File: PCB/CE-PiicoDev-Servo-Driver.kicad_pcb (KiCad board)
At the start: 2 copper layers, 25.4 x 52 mm, 36 parts, among them J1 , J2 , J3 Conn_01x03_Male, J4 Conn_01x03_Male, J5 Conn_01x03_Male, J6 Conn_01x02_Male, J7 Conn_01x02_Male, J8 USB_C_Receptacle_USB2.0, J9 USB_C_Receptacle_USB2.0, U1 PCA9685PW

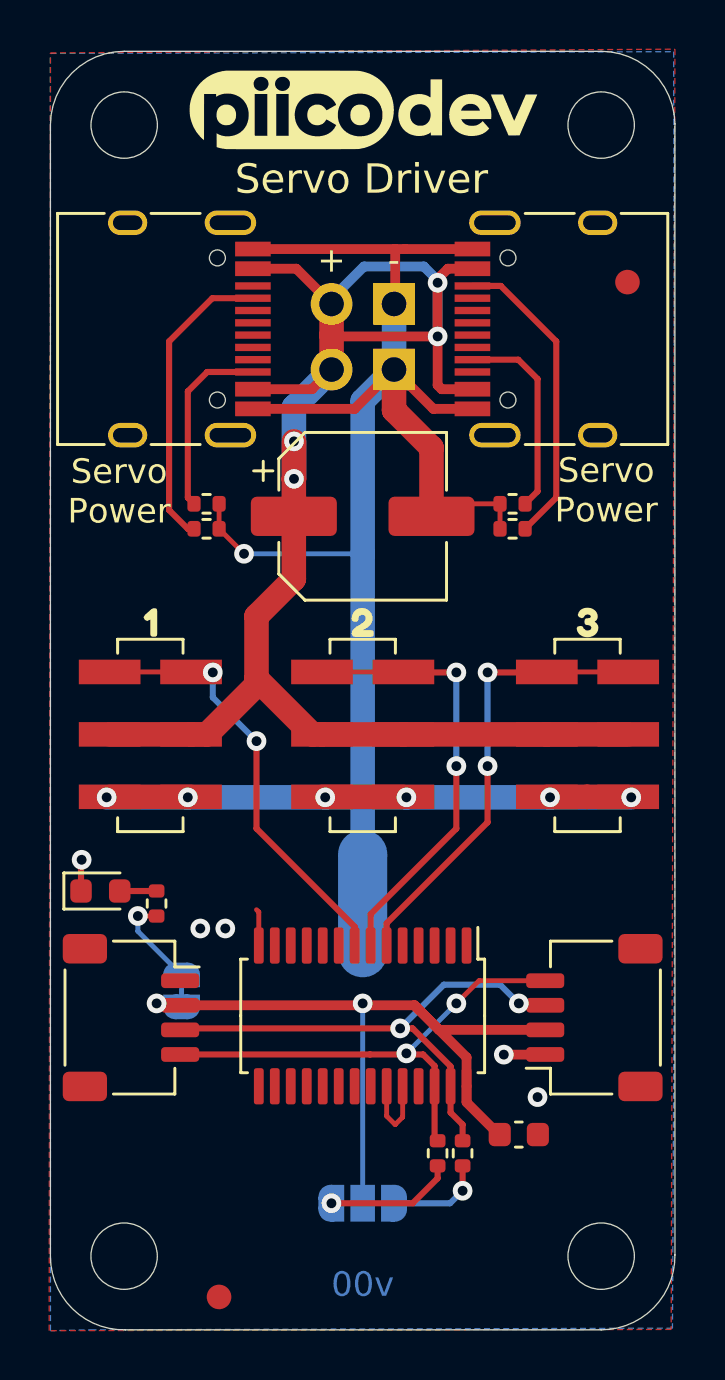
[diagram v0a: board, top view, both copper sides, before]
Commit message: include paste on USB connector support tabs
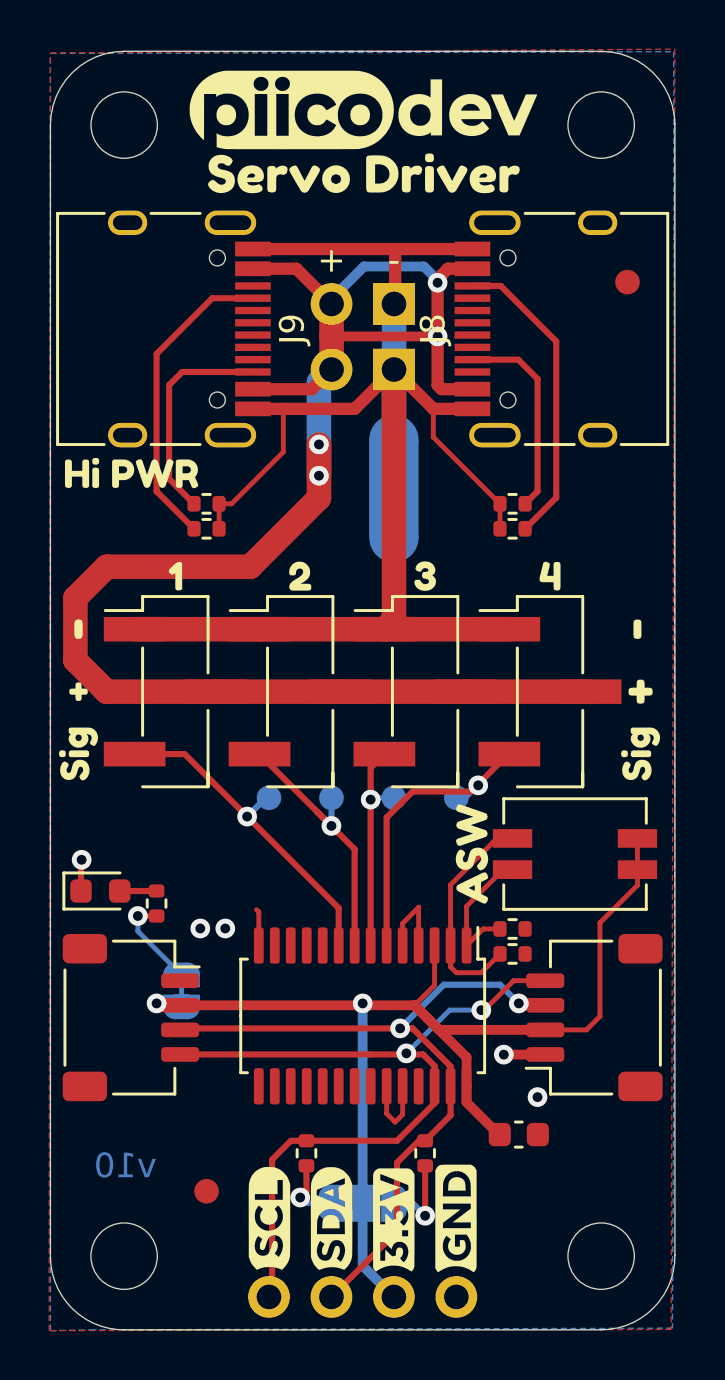
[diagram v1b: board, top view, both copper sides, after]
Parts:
- removed C1: 47u, Capacitor_SMD:CP_Elec_6.3x5.3
- added J10: Breakout Header, CoreElectronics_Components:PiicoDev_header_4pin, F.Cu at (101.1, 112.7)
- added J11: Conn_01x03_Male, Connector_PinHeader_2.54mm:PinHeader_1x03_P2.54mm_Vertical_SMD_Pin1Left, F.Cu at (89.7, 88.1)
- added R8: 10k, Resistor_SMD:R_0402_1005Metric, F.Cu at (103.4, 97.7)
- added R9: 10k, Resistor_SMD:R_0402_1005Metric, F.Cu at (103.4, 98.8)
- added SW1: SW_DIP_x02, CoreElectronics_Components:SW_DIP_x02_Slide_CHS-02A1, F.Cu at (105.9, 94.7)
- added TP1: TestPoint, TestPoint:TestPoint_Pad_D1.0mm, B.Cu at (96.0, 92.4)
- added TP2: TestPoint, TestPoint:TestPoint_Pad_D1.0mm, B.Cu at (98.6, 92.4)
- added TP3: TestPoint, TestPoint:TestPoint_Pad_D1.0mm, B.Cu at (101.1, 92.4)
- added TP4: TestPoint, TestPoint:TestPoint_Pad_D1.0mm, B.Cu at (93.5, 92.4)
- added kibuzzard-6377139C: G***, kibuzzard-6377139C, F.Cu at (104.9, 83.4)
- added kibuzzard-63771600: G***, kibuzzard-63771600, F.Cu at (85.7, 90.6)
- added kibuzzard-63771600: G***, kibuzzard-63771600, F.Cu at (108.6, 90.6)
- added kibuzzard-637721F3: G***, kibuzzard-637721F3, F.Cu at (87.9, 79.2)
- added kibuzzard-637AE2C2: G***, kibuzzard-637AE2C2, F.Cu at (108.6, 88.1)
- added kibuzzard-637AE2C9: G***, kibuzzard-637AE2C9, F.Cu at (108.5, 85.5)
- added kibuzzard-637AE2D0: G***, kibuzzard-637AE2D0, F.Cu at (85.7, 88.1)
- added kibuzzard-637AE2D7: G***, kibuzzard-637AE2D7, F.Cu at (85.7, 85.5)
- added kibuzzard-637AE34A: G***, kibuzzard-637AE34A, F.Cu at (97.3, 67.0)
- added kibuzzard-637AE425: G***, kibuzzard-637AE425, B.Cu at (97.3, 103.9)
- added kibuzzard-637AE445: G***, kibuzzard-637AE445, B.Cu at (97.3, 107.1)
- added kibuzzard-637AE45C: G***, kibuzzard-637AE45C, B.Cu at (86.9, 100.3)
- added kibuzzard-637AE519: G***, kibuzzard-637AE519, B.Cu at (96.3, 81.2)
- added kibuzzard-637AE520: G***, kibuzzard-637AE520, B.Cu at (94.1, 80.0)
- added kibuzzard-637AE527: G***, kibuzzard-637AE527, B.Cu at (92.2, 81.2)
- added kibuzzard-637AE581: G***, kibuzzard-637AE581, B.Cu at (92.2, 86.8)
- added kibuzzard-637AE581: G***, kibuzzard-637AE581, B.Cu at (96.3, 84.8)
- added kibuzzard-637AE581: G***, kibuzzard-637AE581, B.Cu at (92.2, 88.9)
- added kibuzzard-637AE581: G***, kibuzzard-637AE581, B.Cu at (96.3, 88.9)
- added kibuzzard-637AE58B: G***, kibuzzard-637AE58B, B.Cu at (92.2, 82.8)
- added kibuzzard-637AE58B: G***, kibuzzard-637AE58B, B.Cu at (96.3, 86.8)
- added kibuzzard-637AE58B: G***, kibuzzard-637AE58B, B.Cu at (92.2, 84.8)
- added kibuzzard-637AE58B: G***, kibuzzard-637AE58B, B.Cu at (96.3, 82.8)
- added kibuzzard-637AE5E5: G***, kibuzzard-637AE5E5, B.Cu at (101.3, 81.2)
- added kibuzzard-637AEE57: G***, kibuzzard-637AEE57, B.Cu at (101.3, 85.8)
- added kibuzzard-637AF282: G***, kibuzzard-637AF282, F.Cu at (101.7, 94.7)
- J3, J4, J5: footprint CoreElectronics_Components:PinHeader_1x03_P2.54mm_Vertical_SMD_Symmetric -> Connector_PinHeader_2.54mm:PinHeader_1x03_P2.54mm_Vertical_SMD_Pin1Left
- J8, J9: footprint Connector_USB:USB_C_Receptacle_HRO_TYPE-C-31-M-12 -> CoreElectronics_Components:USB_C_Receptacle_HRO_TYPE-C-31-M-12-with-paste
- moved LOGO1 17.3 mm to (108.0, 107.1)
- moved NT1 16.9 mm to (98.6, 79.8)
- moved G2 9.95 mm to (97.3, 98.0)
- moved kibuzzard-6360812A 6.87 mm to (99.8, 83.4)
- moved J3 6.34 mm to (94.7, 88.1)
- moved R2 5.33 mm to (95.0, 106.9)
- moved FID1 4.33 mm to (90.9, 108.4)
- moved kibuzzard-6360811E 3.16 mm to (94.7, 83.4)
- moved J4 3.09 mm to (99.8, 88.1)
- moved J5 2.33 mm to (104.9, 88.1)
- moved kibuzzard-63608105 2.14 mm to (89.7, 83.4)
- moved R3 1.52 mm to (99.8, 106.9)
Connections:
- J3 pad 1: /SERVO1 -> GNDPWR
- J3 pad 3: GNDPWR -> /SERVO2
- J4 pad 1: /SERVO2 -> GNDPWR
- J4 pad 3: GNDPWR -> /SERVO3
- J5 pad 1: /SERVO3 -> GNDPWR
- J5 pad 3: GNDPWR -> /SERVO4
- U1 pad 1: GND -> Net-(R8-Pad1)
- U1 pad 2: GND -> Net-(R9-Pad1)
- U1 pad 3: GND -> +3V3
- U1 pad 6: /SERVO3 -> /SERVO4
- U1 pad 7: /SERVO2 -> /SERVO3
- U1 pad 8: /SERVO1 -> /SERVO2
- U1 pad 9: unconnected-(U1-Pad9) -> /SERVO1
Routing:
- net GNDPWR: track 93.5 -> 65.2 mm, vias 7 -> 0
- net +3V3: track 32.4 -> 49.6 mm
- net /SERVO4: track 0.00 -> 12.4 mm, vias 0 -> 1
- net /SCL: track 22.0 -> 33.6 mm
- net /SERVO3: track 18.5 -> 8.99 mm, vias 2 -> 1
- net Net-(R9-Pad1): track 0.00 -> 9.07 mm
- net /SDA: track 21.9 -> 30.2 mm
- net /SERVO2: track 18.0 -> 11.3 mm, vias 2 -> 1
- net Net-(R8-Pad1): track 0.00 -> 5.62 mm
- net /SERVO1: track 17.7 -> 13.7 mm, vias 2 -> 1
- net +5V: track 68.6 -> 72.4 mm
- net GND: track 8.35 -> 11.5 mm
- net Net-(JP2-Pad3): track 5.24 -> 2.73 mm
- net Net-(J9-PadB5): track 7.65 -> 8.88 mm
- net Net-(JP2-Pad1): track 3.99 -> 3.48 mm
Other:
- board text added: "Designed at Core Electronics by Michael Ruppe November 2022"
- board text added: "v10"
- board text removed: "Designed at Core Electronics by FIRSTNAME LASTNAME MONTHNAME YYYY"
- board text removed: "I2C PU"
- board text removed: "PWR LED"
- board text removed: "Servo Driver"
- board text removed: "Servo Power"
- board text removed: "piico.dev/p29"
- board text removed: "v00"
